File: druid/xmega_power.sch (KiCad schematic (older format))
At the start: 11 parts, among them U4 XC6206P332MR

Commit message: - Переделана клавиатура - установлены все корпуса микросхем
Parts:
- C24, C25, C26, C27, C28, C29, C30, C31: footprint (none) -> Capacitors_SMD:C_1206_HandSoldering; symbol C -> C-RESCUE-xmobile
- D11: footprint (none) -> Diodes_SMD:SMA_Handsoldering; symbol ZENER -> ZENER-RESCUE-xmobile
- L2: footprint (none) -> Inductors:Inductor_1212
- U4: footprint MODULE -> TO_SOT_Packages_SMD:SOT-23
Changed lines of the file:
@@
 EESchema Schematic File Version 2
+LIBS:xmobile-rescue
 LIBS:power
 LIBS:device
@@
 LIBS:contrib
 LIBS:valves
-LIBS:zakadc
-LIBS:vw2500m
-LIBS:usb-b
-LIBS:uprojects-msp430
-LIBS:uprojects-maxim-integrated
-LIBS:tps79530
-LIBS:tps63001
-LIBS:tps61040dbv
-LIBS:tact_sw
-LIBS:str751fr0t6
-LIBS:stm32f103cb
-LIBS:stm32f101cbt6
-LIBS:stm32f030f4
-LIBS:stm32f20x_LQFP64
-LIBS:sn54ac04
-LIBS:smf05c
-LIBS:sim_holder
-LIBS:sim900
-LIBS:sim800c
-LIBS:reset_supervisor
-LIBS:quectel
-LIBS:psl-ecg_12md_ads1298
-LIBS:pl2303
-LIBS:pcf8563_rtc
-LIBS:opa333_sot23-5
-LIBS:nrf8001
-LIBS:ncp3020
-LIBS:mt3608
-LIBS:molex_sim_holder_47553
-LIBS:micro_usb_b
-LIBS:microsd_socket
-LIBS:md1506_gsm_ant
-LIBS:mcp73833
-LIBS:mcp73831
-LIBS:mb6s
-LIBS:max669
-LIBS:ltc4120
-LIBS:ltc3533
-LIBS:lt1370
-LIBS:lpc1313
-LIBS:lp2951
-LIBS:lm2931cdr2g
-LIBS:lm809
-LIBS:lis3dh
-LIBS:led_couple
-LIBS:l6984
-LIBS:itg3200
-LIBS:irfh9310
-LIBS:irfh5300
-LIBS:ir2110l4
-LIBS:hmc5883
-LIBS:hlk-rm04
-LIBS:hc735-oscillator
-LIBS:gl850g_usb_hub
-LIBS:esp-07
-LIBS:dpak-diode
-LIBS:cstce_crystal
-LIBS:conn15
-LIBS:cc3100mod
-LIBS:bmp180
-LIBS:ble112
-LIBS:alt_symbols
-LIBS:ads1298_ecg_adc
-LIBS:ad8542
-LIBS:ad8495
-LIBS:ad8054
-LIBS:ad8051
-LIBS:3225_4p_quartz
-LIBS:74lvc02
 LIBS:XC6206P332MR
 LIBS:STF202-22T1G
 LIBS:MCP73871
+LIBS:switch1
 LIBS:xmobile-cache
 EELAYER 25 0
@@
 $EndDescr
 $Comp
-L +BATT #PWR2
+L +BATT #PWR01
 U 1 1 5A9FD1BA
 P 4625 5250
-F 0 "#PWR2" H 4625 5200 20  0001 C CNN
+F 0 "#PWR01" H 4625 5200 20  0001 C CNN
 F 1 "+BATT" H 4625 5350 30  0000 C CNN
 F 2 "" H 4625 5250 60  0001 C CNN
@@
 F 0 "L2" V 7700 2250 40  0000 C CNN
 F 1 "10mk" V 7850 2250 40  0000 C CNN
-F 2 "" H 7750 2250 60  0000 C CNN
+F 2 "Inductors:Inductor_1212" H 7750 2250 60  0000 C CNN
 F 3 "" H 7750 2250 60  0000 C CNN
 	1    7750 2250
@@
 $EndComp
 $Comp
-L C C31
+L C-RESCUE-xmobile C31
 U 1 1 5A9FD1C7
 P 7250 2800
 F 0 "C31" H 7250 2900 40  0000 L CNN
 F 1 "100n" H 7256 2715 40  0000 L CNN
-F 2 "" H 7288 2650 30  0000 C CNN
+F 2 "Capacitors_SMD:C_1206_HandSoldering" H 7288 2650 30  0000 C CNN
 F 3 "" H 7250 2800 60  0000 C CNN
 	1    7250 2800
@@
 $EndComp
 $Comp
-L C C30
+L C-RESCUE-xmobile C30
 U 1 1 5A9FD1CE
 P 6950 2800
 F 0 "C30" H 6950 2900 40  0000 L CNN
 F 1 "47mk" H 6956 2715 40  0000 L CNN
-F 2 "" H 6988 2650 30  0000 C CNN
+F 2 "Capacitors_SMD:C_1206_HandSoldering" H 6988 2650 30  0000 C CNN
 F 3 "" H 6950 2800 60  0000 C CNN
 	1    6950 2800
@@
 $EndComp
 $Comp
-L C C29
+L C-RESCUE-xmobile C29
 U 1 1 5A9FD1D5
 P 6675 2800
 F 0 "C29" H 6675 2900 40  0000 L CNN
 F 1 "1mk (ceramic)" H 6681 2715 40  0000 L CNN
-F 2 "" H 6713 2650 30  0000 C CNN
+F 2 "Capacitors_SMD:C_1206_HandSoldering" H 6713 2650 30  0000 C CNN
 F 3 "" H 6675 2800 60  0000 C CNN
 	1    6675 2800
@@
 $EndComp
 $Comp
-L C C24
+L C-RESCUE-xmobile C24
 U 1 1 5A9FD1DC
 P 4775 2450
 F 0 "C24" H 4775 2550 40  0000 L CNN
 F 1 "1mk (ceramic)" H 4781 2365 40  0000 L CNN
-F 2 "" H 4813 2300 30  0000 C CNN
+F 2 "Capacitors_SMD:C_1206_HandSoldering" H 4813 2300 30  0000 C CNN
 F 3 "" H 4775 2450 60  0000 C CNN
 	1    4775 2450
@@
 $EndComp
 $Comp
-L GND #PWR3
+L GND-RESCUE-xmobile #PWR02
 U 1 1 5A9FD1E3
 P 5650 4125
-F 0 "#PWR3" H 5650 4125 30  0001 C CNN
+F 0 "#PWR02" H 5650 4125 30  0001 C CNN
 F 1 "GND" H 5650 4055 30  0001 C CNN
 F 2 "" H 5650 4125 60  0001 C CNN
@@
 $EndComp
 $Comp
-L C C25
+L C-RESCUE-xmobile C25
 U 1 1 5A9FD1E9
 P 4950 5575
 F 0 "C25" H 4950 5675 40  0000 L CNN
 F 1 "100mk (tantal)" H 4800 5450 40  0000 L CNN
-F 2 "" H 4988 5425 30  0000 C CNN
+F 2 "Capacitors_SMD:C_1206_HandSoldering" H 4988 5425 30  0000 C CNN
 F 3 "" H 4950 5575 60  0000 C CNN
 	1    4950 5575
@@
 $EndComp
 $Comp
-L C C26
+L C-RESCUE-xmobile C26
 U 1 1 5A9FD1F0
 P 5425 5575
 F 0 "C26" H 5425 5675 40  0000 L CNN
 F 1 "10mk (ceramic)" H 5225 5500 40  0000 L CNN
-F 2 "" H 5463 5425 30  0000 C CNN
+F 2 "Capacitors_SMD:C_1206_HandSoldering" H 5463 5425 30  0000 C CNN
 F 3 "" H 5425 5575 60  0000 C CNN
 	1    5425 5575
@@
 $EndComp
 $Comp
-L C C27
+L C-RESCUE-xmobile C27
 U 1 1 5A9FD1F7
 P 5850 5575
 F 0 "C27" H 5850 5675 40  0000 L CNN
 F 1 "33p" H 5856 5490 40  0000 L CNN
-F 2 "" H 5888 5425 30  0000 C CNN
+F 2 "Capacitors_SMD:C_1206_HandSoldering" H 5888 5425 30  0000 C CNN
 F 3 "" H 5850 5575 60  0000 C CNN
 	1    5850 5575
@@
 $EndComp
 $Comp
-L C C28
+L C-RESCUE-xmobile C28
 U 1 1 5A9FD1FE
 P 6225 5575
 F 0 "C28" H 6225 5675 40  0000 L CNN
 F 1 "10p" H 6231 5490 40  0000 L CNN
-F 2 "" H 6263 5425 30  0000 C CNN
+F 2 "Capacitors_SMD:C_1206_HandSoldering" H 6263 5425 30  0000 C CNN
 F 3 "" H 6225 5575 60  0000 C CNN
 	1    6225 5575
@@
 F 0 "U4" H 5700 2200 50  0000 C CNN
 F 1 "XC6206P332MR" H 5700 2600 50  0000 C CNN
-F 2 "MODULE" H 5700 2300 50  0001 C CNN
+F 2 "TO_SOT_Packages_SMD:SOT-23" H 5700 2300 50  0001 C CNN
 F 3 "DOCUMENTATION" H 5700 2300 50  0001 C CNN
 	1    5700 2300
@@
 GND
 $Comp
-L ZENER D11
+L ZENER-RESCUE-xmobile D11
 U 1 1 5A9FD218
 P 6550 5575
 F 0 "D11" H 6550 5675 50  0000 C CNN
 F 1 "ZENER" H 6550 5475 40  0000 C CNN
-F 2 "" H 6550 5575 60  0000 C CNN
+F 2 "Diodes_SMD:SMA_Handsoldering" H 6550 5575 60  0000 C CNN
 F 3 "" H 6550 5575 60  0000 C CNN
 	1    6550 5575
@@
 	4650 5875 6550 5875
 $Comp
-L +BATT #PWR1
+L +BATT #PWR03
 U 1 1 5A9FE80A
 P 4500 2250
-F 0 "#PWR1" H 4500 2200 20  0001 C CNN
+F 0 "#PWR03" H 4500 2200 20  0001 C CNN
 F 1 "+BATT" H 4500 2350 30  0000 C CNN
 F 2 "" H 4500 2250 60  0001 C CNN

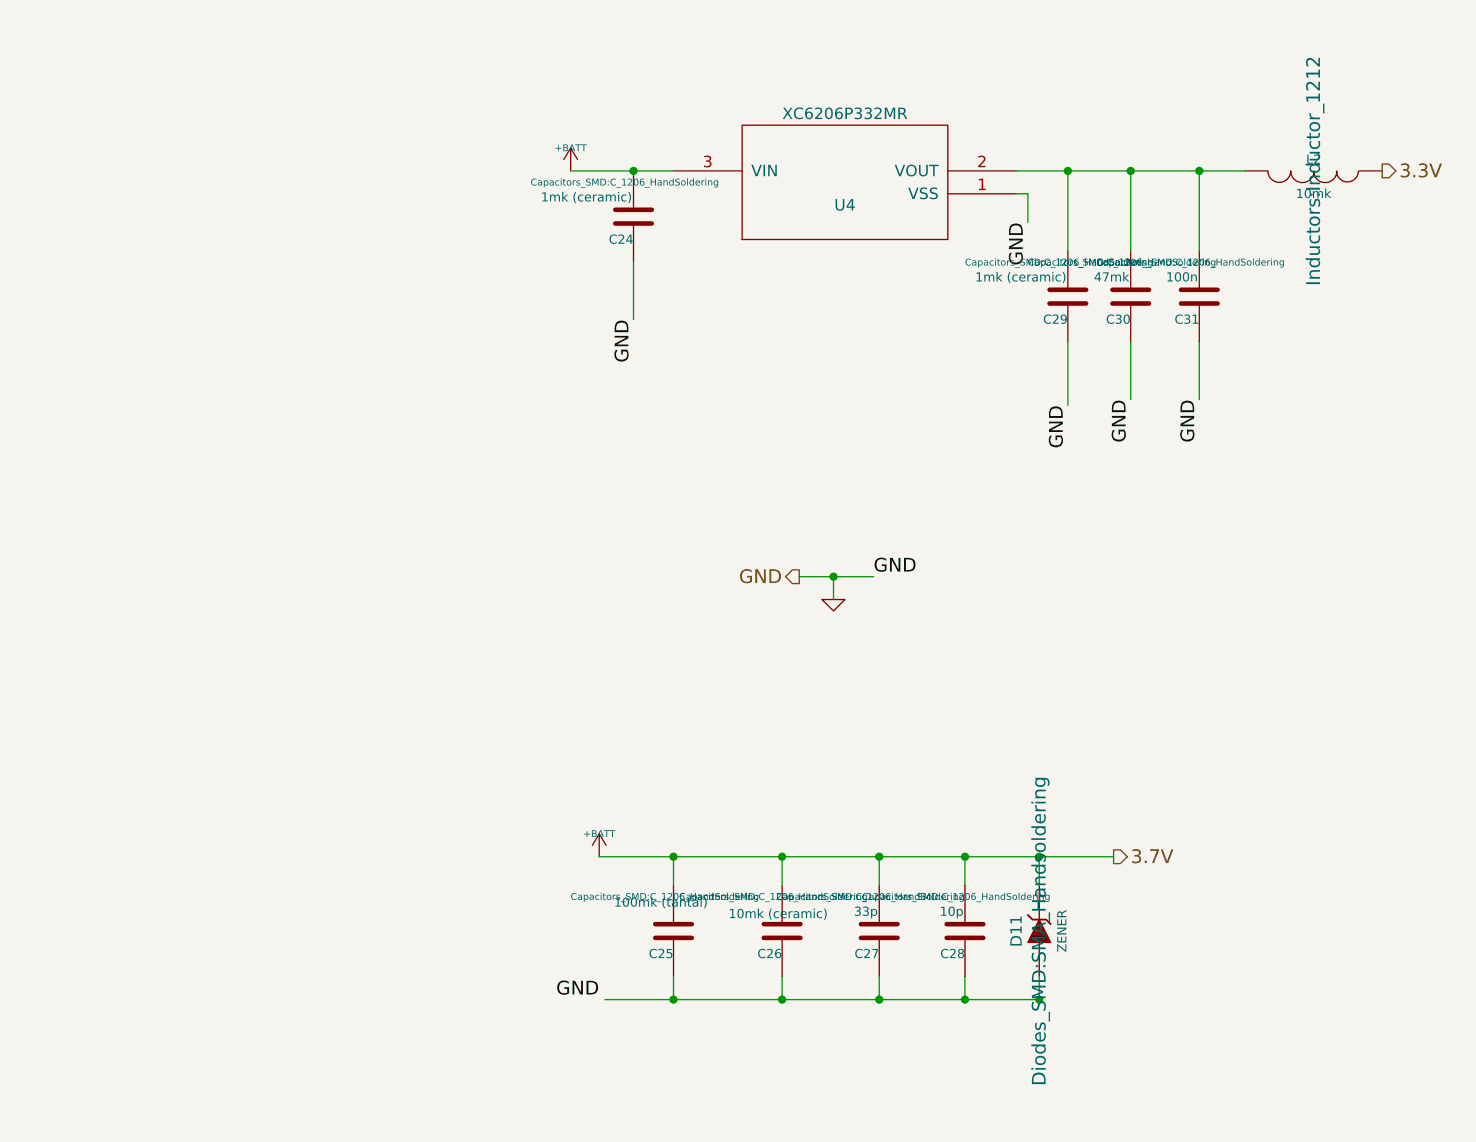
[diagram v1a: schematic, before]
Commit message: Исправлины все ошибки и предупреждения в электрической схеме
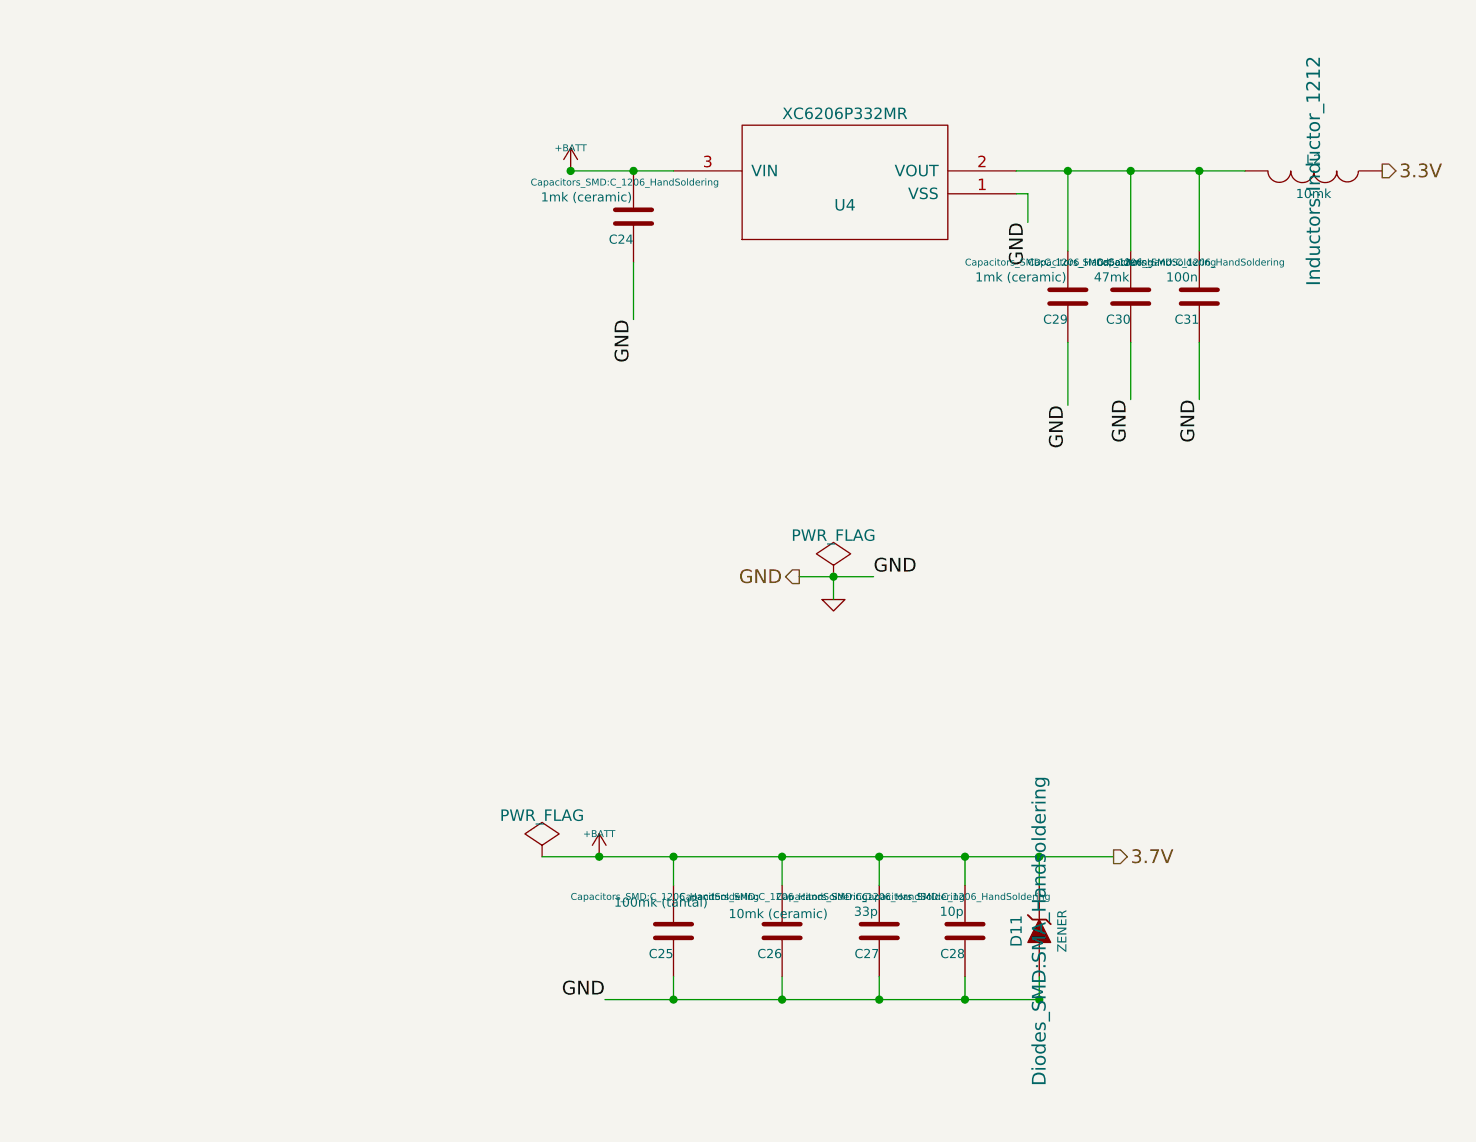
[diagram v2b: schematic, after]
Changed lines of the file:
@@
 $EndDescr
 $Comp
-L +BATT #PWR01
+L +BATT #PWR03
 U 1 1 5A9FD1BA
 P 4625 5250
-F 0 "#PWR01" H 4625 5200 20  0001 C CNN
+F 0 "#PWR03" H 4625 5200 20  0001 C CNN
 F 1 "+BATT" H 4625 5350 30  0000 C CNN
 F 2 "" H 4625 5250 60  0001 C CNN
@@
 $EndComp
 $Comp
-L GND-RESCUE-xmobile #PWR02
+L GND-RESCUE-xmobile #PWR04
 U 1 1 5A9FD1E3
 P 5650 4125
-F 0 "#PWR02" H 5650 4125 30  0001 C CNN
+F 0 "#PWR04" H 5650 4125 30  0001 C CNN
 F 1 "GND" H 5650 4055 30  0001 C CNN
 F 2 "" H 5650 4125 60  0001 C CNN
@@
 Text Label 4775 2900 3    60   ~ 0
 GND
-Text Label 4625 5875 2    60   ~ 0
+Text Label 4650 5875 2    60   ~ 0
 GND
 $Comp
@@
 Connection ~ 6675 2250
 Wire Wire Line
-	4500 2250 4950 2250
-Wire Wire Line
 	6450 2350 6500 2350
 Wire Wire Line
@@
 	7250 2600 7250 2250
 Wire Wire Line
-	4625 5250 6875 5250
+	4375 5250 6875 5250
 Wire Wire Line
 	4950 5775 4950 5875
@@
 	4650 5875 6550 5875
 $Comp
-L +BATT #PWR03
+L +BATT #PWR05
 U 1 1 5A9FE80A
 P 4500 2250
-F 0 "#PWR03" H 4500 2200 20  0001 C CNN
+F 0 "#PWR05" H 4500 2200 20  0001 C CNN
 F 1 "+BATT" H 4500 2350 30  0000 C CNN
 F 2 "" H 4500 2250 60  0001 C CNN
@@
 GND
 Connection ~ 5650 4025
+Connection ~ 4500 2250
+$Comp
+L PWR_FLAG #FLG06
+U 1 1 5AB7534F
+P 4375 5250
+F 0 "#FLG06" H 4375 5345 50  0001 C CNN
+F 1 "PWR_FLAG" H 4375 5430 50  0000 C CNN
+F 2 "" H 4375 5250 50  0000 C CNN
+F 3 "" H 4375 5250 50  0000 C CNN
+	1    4375 5250
+	1    0    0    -1
+$EndComp
+Connection ~ 4625 5250
+$Comp
+L PWR_FLAG #FLG07
+U 1 1 5AB75478
+P 5650 4025
+F 0 "#FLG07" H 5650 4120 50  0001 C CNN
+F 1 "PWR_FLAG" H 5650 4205 50  0000 C CNN
+F 2 "" H 5650 4025 50  0000 C CNN
+F 3 "" H 5650 4025 50  0000 C CNN
+	1    5650 4025
+	1    0    0    -1
+$EndComp
+Wire Wire Line
+	4950 2250 4500 2250
 $EndSCHEMATC

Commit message: Переместил посадочные места по кучкам
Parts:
- added P8, P9: CONN_01X02, Connectors_Hirose:Hirose_DF13-02P-1.25DSA_02x1.25mm_Straight, symbol CONN_01X02
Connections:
- net +BATT: now also P8.2 (P2), P9.2 (P2)
- net GND: now also P8.1 (P1), P9.1 (P1)
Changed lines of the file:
@@
 $EndDescr
 $Comp
-L +BATT #PWR03
+L +BATT #PWR2
 U 1 1 5A9FD1BA
 P 4625 5250
-F 0 "#PWR03" H 4625 5200 20  0001 C CNN
+F 0 "#PWR2" H 4625 5200 20  0001 C CNN
 F 1 "+BATT" H 4625 5350 30  0000 C CNN
 F 2 "" H 4625 5250 60  0001 C CNN
@@
 $EndComp
 $Comp
-L GND-RESCUE-xmobile #PWR04
+L GND-RESCUE-xmobile #PWR3
 U 1 1 5A9FD1E3
 P 5650 4125
-F 0 "#PWR04" H 5650 4125 30  0001 C CNN
+F 0 "#PWR3" H 5650 4125 30  0001 C CNN
 F 1 "GND" H 5650 4055 30  0001 C CNN
 F 2 "" H 5650 4125 60  0001 C CNN
@@
 	7250 2600 7250 2250
 Wire Wire Line
-	4375 5250 6875 5250
+	3900 5250 6875 5250
 Wire Wire Line
 	4950 5775 4950 5875
@@
 	4650 5875 6550 5875
 $Comp
-L +BATT #PWR05
+L +BATT #PWR1
 U 1 1 5A9FE80A
 P 4500 2250
-F 0 "#PWR05" H 4500 2200 20  0001 C CNN
+F 0 "#PWR1" H 4500 2200 20  0001 C CNN
 F 1 "+BATT" H 4500 2350 30  0000 C CNN
 F 2 "" H 4500 2250 60  0001 C CNN
@@
 Connection ~ 4500 2250
 $Comp
-L PWR_FLAG #FLG06
+L PWR_FLAG #FLG3
 U 1 1 5AB7534F
 P 4375 5250
-F 0 "#FLG06" H 4375 5345 50  0001 C CNN
+F 0 "#FLG3" H 4375 5345 50  0001 C CNN
 F 1 "PWR_FLAG" H 4375 5430 50  0000 C CNN
 F 2 "" H 4375 5250 50  0000 C CNN
@@
 Connection ~ 4625 5250
 $Comp
-L PWR_FLAG #FLG07
+L PWR_FLAG #FLG4
 U 1 1 5AB75478
 P 5650 4025
-F 0 "#FLG07" H 5650 4120 50  0001 C CNN
+F 0 "#FLG4" H 5650 4120 50  0001 C CNN
 F 1 "PWR_FLAG" H 5650 4205 50  0000 C CNN
 F 2 "" H 5650 4025 50  0000 C CNN
@@
 $EndComp
 Wire Wire Line
-	4950 2250 4500 2250
+	4050 2250 4950 2250
+Connection ~ 4375 5250
+$Comp
+L CONN_01X02 P9
+U 1 1 5AB7EB32
+P 3650 2650
+F 0 "P9" H 3650 2800 50  0000 C CNN
+F 1 "CONN_01X02" V 3750 2650 50  0000 C CNN
+F 2 "Connectors_Hirose:Hirose_DF13-02P-1.25DSA_02x1.25mm_Straight" H 3650 2650 50  0000 C CNN
+F 3 "" H 3650 2650 50  0000 C CNN
+	1    3650 2650
+	-1   0    0    1
+$EndComp
+Wire Wire Line
+	3850 2600 4050 2600
+Wire Wire Line
+	4050 2600 4050 2250
+Wire Wire Line
+	3850 2700 4775 2700
+Connection ~ 4775 2700
+$Comp
+L CONN_01X02 P8
+U 1 1 5AB7ED0D
+P 3575 5550
+F 0 "P8" H 3575 5700 50  0000 C CNN
+F 1 "CONN_01X02" V 3675 5550 50  0000 C CNN
+F 2 "Connectors_Hirose:Hirose_DF13-02P-1.25DSA_02x1.25mm_Straight" H 3575 5550 50  0000 C CNN
+F 3 "" H 3575 5550 50  0000 C CNN
+	1    3575 5550
+	-1   0    0    1
+$EndComp
+Wire Wire Line
+	3775 5500 3900 5500
+Wire Wire Line
+	3900 5500 3900 5250
+Wire Wire Line
+	3775 5600 4700 5600
+Wire Wire Line
+	4700 5600 4700 5875
+Connection ~ 4700 5875
 $EndSCHEMATC

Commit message: Заменил посадочные места для некоторых контактных расчёсок
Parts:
- P8, P9: footprint Connectors_Hirose:Hirose_DF13-02P-1.25DSA_02x1.25mm_Straight -> Connectors_JAE:JAE_LY20-08P-2T_2x04x2.00mm_Straight
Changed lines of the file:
@@
 $EndDescr
 $Comp
-L +BATT #PWR2
+L +BATT #PWR03
 U 1 1 5A9FD1BA
 P 4625 5250
-F 0 "#PWR2" H 4625 5200 20  0001 C CNN
+F 0 "#PWR03" H 4625 5200 20  0001 C CNN
 F 1 "+BATT" H 4625 5350 30  0000 C CNN
 F 2 "" H 4625 5250 60  0001 C CNN
@@
 $EndComp
 $Comp
-L GND-RESCUE-xmobile #PWR3
+L GND-RESCUE-xmobile #PWR04
 U 1 1 5A9FD1E3
 P 5650 4125
-F 0 "#PWR3" H 5650 4125 30  0001 C CNN
+F 0 "#PWR04" H 5650 4125 30  0001 C CNN
 F 1 "GND" H 5650 4055 30  0001 C CNN
 F 2 "" H 5650 4125 60  0001 C CNN
@@
 	4650 5875 6550 5875
 $Comp
-L +BATT #PWR1
+L +BATT #PWR05
 U 1 1 5A9FE80A
 P 4500 2250
-F 0 "#PWR1" H 4500 2200 20  0001 C CNN
+F 0 "#PWR05" H 4500 2200 20  0001 C CNN
 F 1 "+BATT" H 4500 2350 30  0000 C CNN
 F 2 "" H 4500 2250 60  0001 C CNN
@@
 Connection ~ 4500 2250
 $Comp
-L PWR_FLAG #FLG3
+L PWR_FLAG #FLG06
 U 1 1 5AB7534F
 P 4375 5250
-F 0 "#FLG3" H 4375 5345 50  0001 C CNN
+F 0 "#FLG06" H 4375 5345 50  0001 C CNN
 F 1 "PWR_FLAG" H 4375 5430 50  0000 C CNN
 F 2 "" H 4375 5250 50  0000 C CNN
@@
 Connection ~ 4625 5250
 $Comp
-L PWR_FLAG #FLG4
+L PWR_FLAG #FLG07
 U 1 1 5AB75478
 P 5650 4025
-F 0 "#FLG4" H 5650 4120 50  0001 C CNN
+F 0 "#FLG07" H 5650 4120 50  0001 C CNN
 F 1 "PWR_FLAG" H 5650 4205 50  0000 C CNN
 F 2 "" H 5650 4025 50  0000 C CNN
@@
 F 0 "P9" H 3650 2800 50  0000 C CNN
 F 1 "CONN_01X02" V 3750 2650 50  0000 C CNN
-F 2 "Connectors_Hirose:Hirose_DF13-02P-1.25DSA_02x1.25mm_Straight" H 3650 2650 50  0000 C CNN
+F 2 "Connectors_JAE:JAE_LY20-08P-2T_2x04x2.00mm_Straight" H 3650 2650 50  0000 C CNN
 F 3 "" H 3650 2650 50  0000 C CNN
 	1    3650 2650
@@
 F 0 "P8" H 3575 5700 50  0000 C CNN
 F 1 "CONN_01X02" V 3675 5550 50  0000 C CNN
-F 2 "Connectors_Hirose:Hirose_DF13-02P-1.25DSA_02x1.25mm_Straight" H 3575 5550 50  0000 C CNN
+F 2 "Connectors_JAE:JAE_LY20-08P-2T_2x04x2.00mm_Straight" H 3575 5550 50  0000 C CNN
 F 3 "" H 3575 5550 50  0000 C CNN
 	1    3575 5550

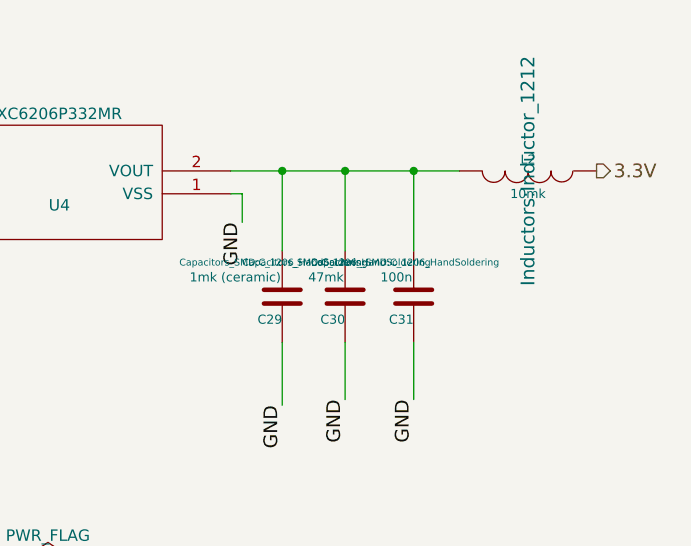
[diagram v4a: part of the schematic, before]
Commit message: зменена посадочная площадка (меньше чем была) лоя кондернасоторв 100n
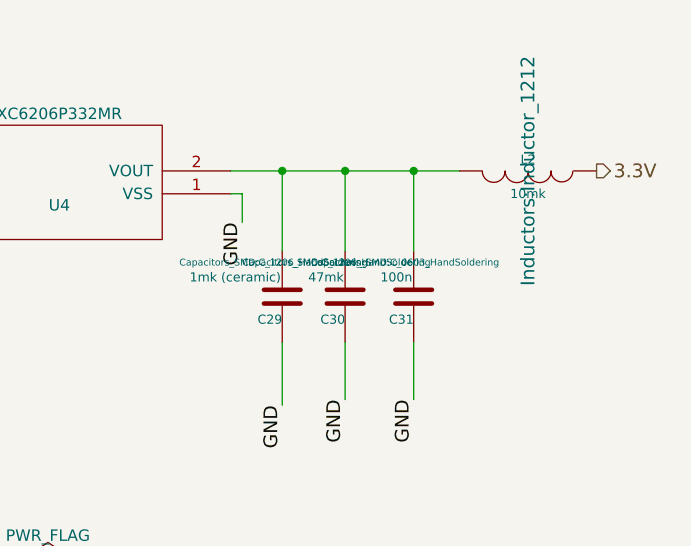
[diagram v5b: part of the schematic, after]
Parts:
- C31: footprint Capacitors_SMD:C_1206_HandSoldering -> Capacitors_SMD:C_0603_HandSoldering
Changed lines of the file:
@@
 F 0 "C31" H 7250 2900 40  0000 L CNN
 F 1 "100n" H 7256 2715 40  0000 L CNN
-F 2 "Capacitors_SMD:C_1206_HandSoldering" H 7288 2650 30  0000 C CNN
+F 2 "Capacitors_SMD:C_0603_HandSoldering" H 7288 2650 30  0000 C CNN
 F 3 "" H 7250 2800 60  0000 C CNN
 	1    7250 2800
